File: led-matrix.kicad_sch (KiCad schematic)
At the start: 91 parts, among them J1 Conn_01x01_Pin, J10 Conn_01x01_Pin, J11 Conn_01x01_Pin, J12 Conn_01x01_Pin, J13 Conn_01x01_Pin, J14 Conn_01x01_Pin, J15 Conn_01x01_Pin, J16 Conn_01x01_Pin, J17 Conn_01x01_Pin, J18 Conn_01x01_Pin, J19 Conn_01x01_Pin, J2 Conn_01x01_Pin, J20 Conn_01x01_Pin, J21 Conn_01x01_Pin, J22 Conn_01x01_Pin, J23 Conn_01x01_Pin, J3 Conn_01x01_Pin, J4 Conn_01x01_Pin, J5 Conn_01x01_Pin, J6 Conn_01x01_Pin, J7 Conn_01x01_Pin, J8 Conn_01x01_Pin, J9 Conn_01x01_Pin, U1 MAX7219, U2 Pico

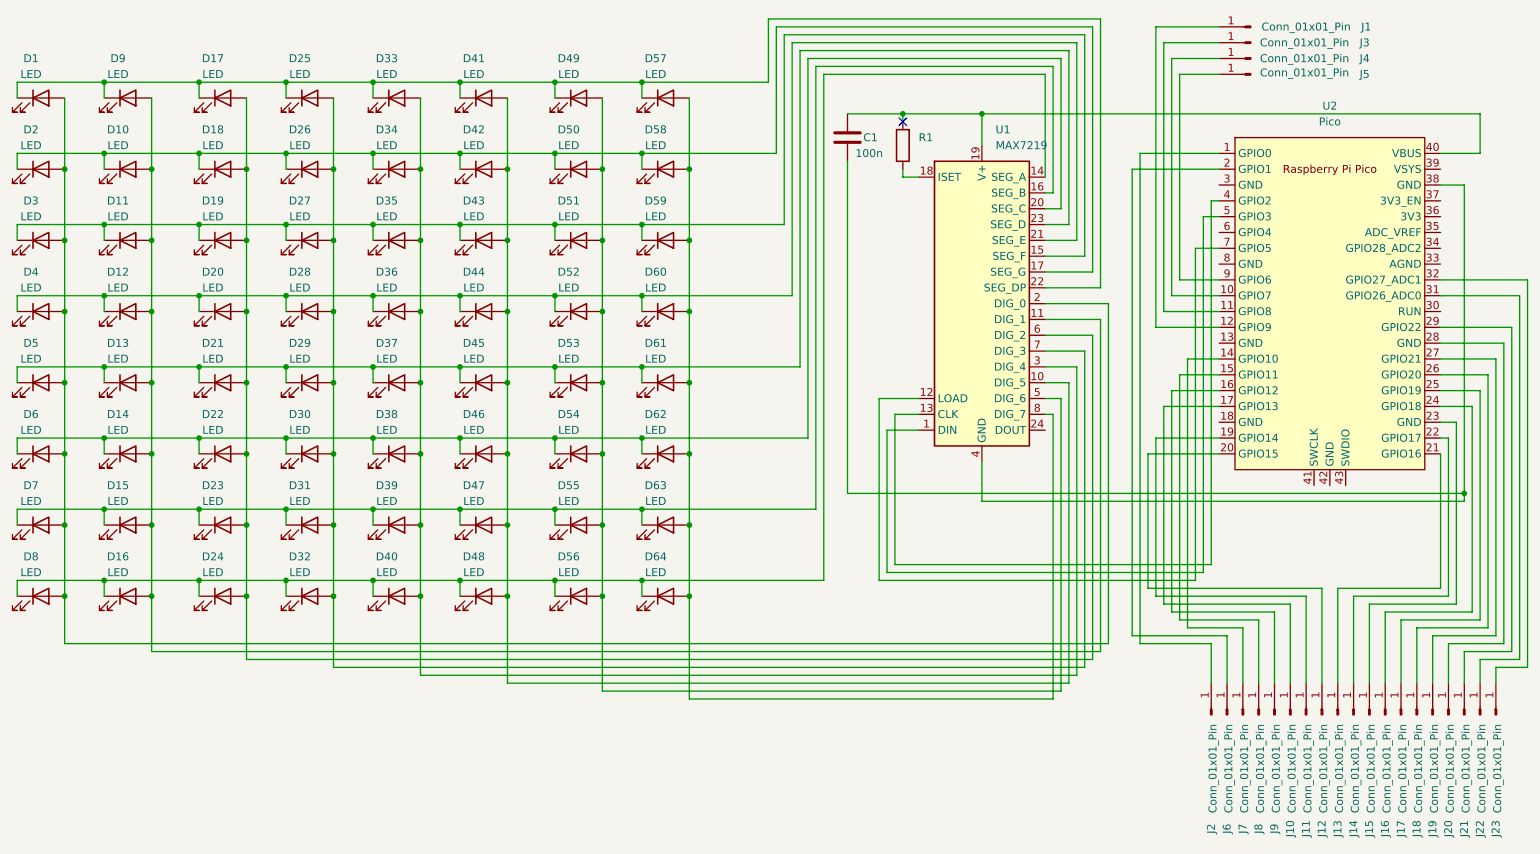
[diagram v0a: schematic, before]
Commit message: chore: remove redundant grounds from gpio
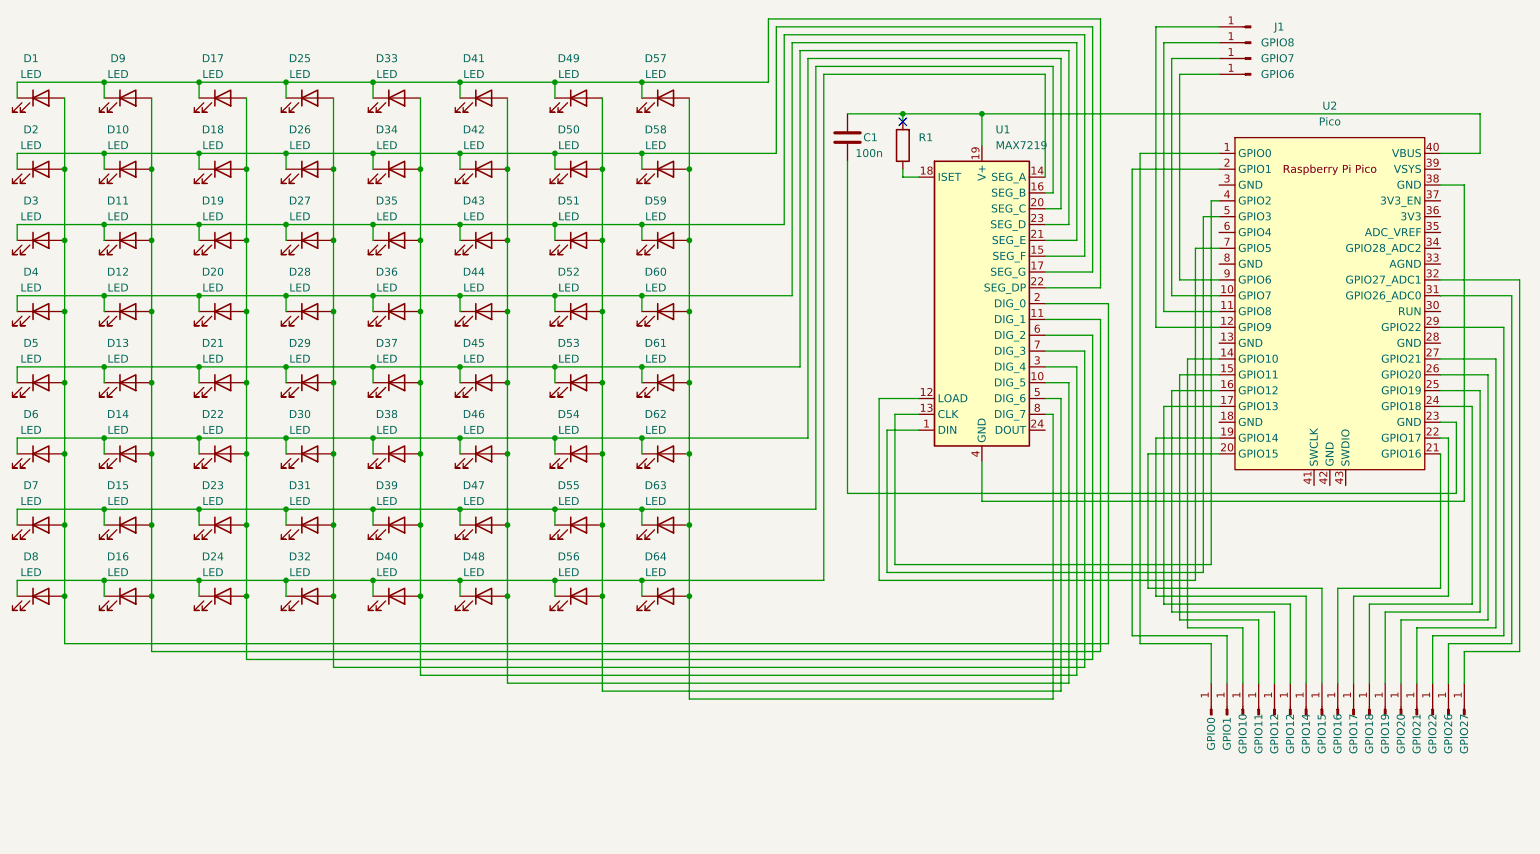
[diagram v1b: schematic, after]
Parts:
- removed J22, J23: Conn_01x01_Pin, Connector_Pin:Pin_D1.2mm_L11.3mm_W3.0mm_Flat, symbol Connector:Conn_01x01_Pin
- renumbered J2 to GPIO0, J6 to GPIO1, J7 to GPIO10, J8 to GPIO11, J10 to GPIO12, J9 to GPIO12, J11 to GPIO14, J12 to GPIO15, J13 to GPIO16, J14 to GPIO17, J15 to GPIO18, J16 to GPIO19, J17 to GPIO20, J18 to GPIO21, J19 to GPIO22, J20 to GPIO26, J21 to GPIO27, J5 to GPIO6, J4 to GPIO7, J3 to GPIO8
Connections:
- net at GPIO27.1 (Pin_1): now also U2.32 (GPIO27_ADC1); no longer U2.29 (GPIO22)
- net at GPIO22.1 (Pin_1): now also U2.29 (GPIO22); no longer U2.27 (GPIO21)
- net at GPIO21.1 (Pin_1): now also U2.27 (GPIO21); no longer U2.26 (GPIO20)
- net at GPIO19.1 (Pin_1): now also U2.25 (GPIO19); no longer U2.24 (GPIO18)
- net at GPIO26.1 (Pin_1): now also U2.31 (GPIO26_ADC0); no longer U2.28 (GND)
- net at GPIO18.1 (Pin_1): now also U2.24 (GPIO18); no longer U2.23 (GND)
- net at U1.4 (GND), U1.9 (GND), U2.38 (GND): no longer C1.2
- net at GPIO20.1 (Pin_1): now also U2.26 (GPIO20); no longer U2.25 (GPIO19)
- new net: C1.2, U2.23 (GND)

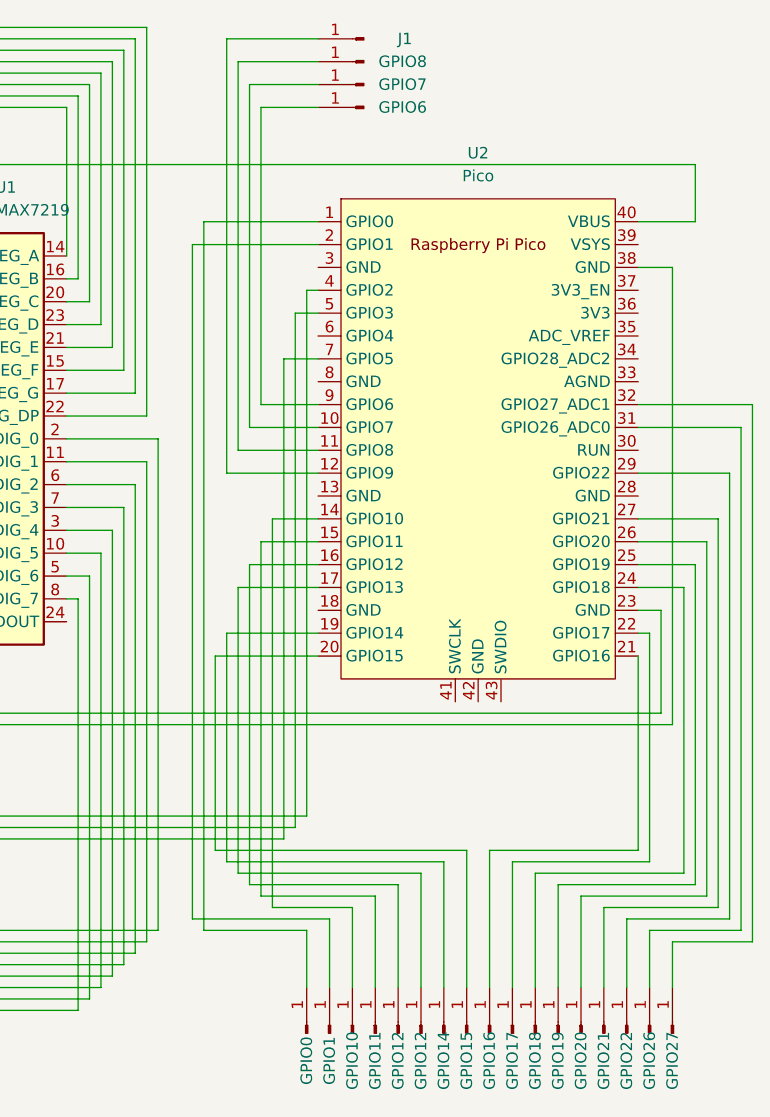
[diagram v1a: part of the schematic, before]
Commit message: feat: change gpio names and move positions on pcb
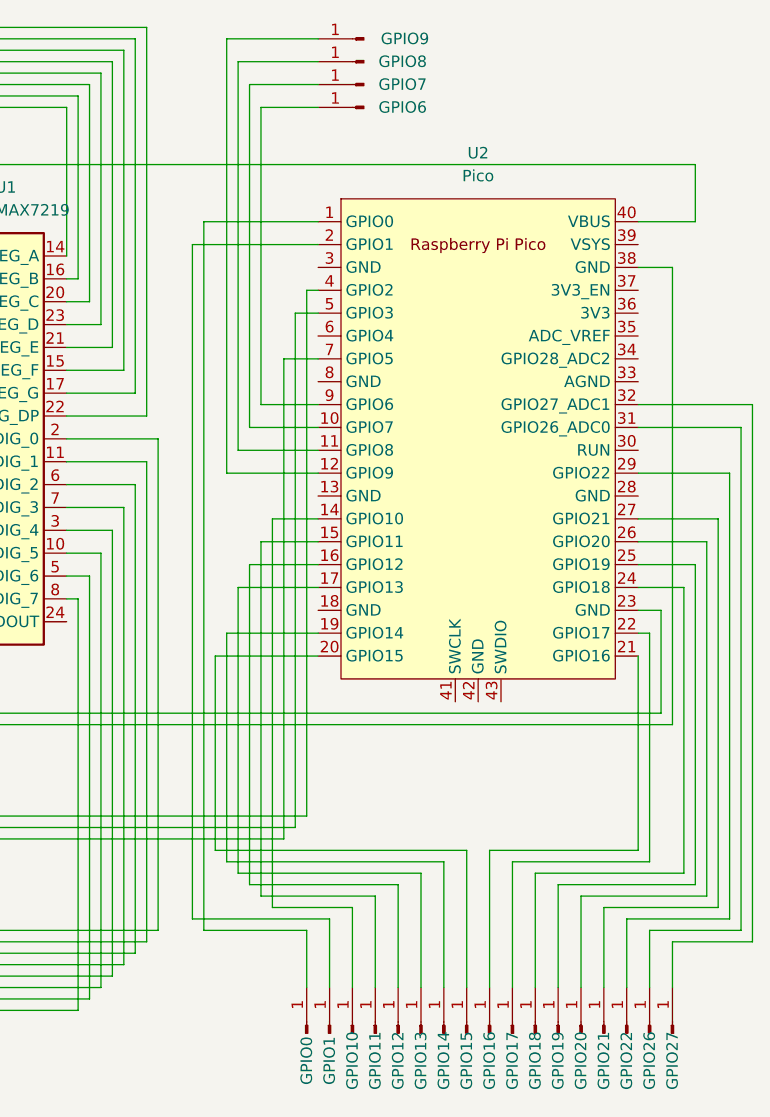
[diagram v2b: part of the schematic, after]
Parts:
- renumbered GPIO12 to GPIO13, J1 to GPIO9
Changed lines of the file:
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@@
 		(on_board yes)
 		(dnp no)
-		(property "Reference" "J1"
+		(property "Reference" "GPIO9"
 			(at 228.092 25.4 0)
 			(effects
@@
 			(project ""
 				(path "/14dbb19e-a51b-4674-aa79-c96e0324fb3f"
-					(reference "J1")
+					(reference "GPIO9")
 					(unit 1)
 				)
@@
 		(on_board yes)
 		(dnp no)
-		(property "Reference" "GPIO12"
+		(property "Reference" "GPIO13"
 			(at 229.87 138.938 0)
 			(effects
@@
 			(project "led-matrix"
 				(path "/14dbb19e-a51b-4674-aa79-c96e0324fb3f"
-					(reference "GPIO12")
-					(unit 1)
-				)
+					(reference "GPIO13")
+					(unit 1)
+				)
